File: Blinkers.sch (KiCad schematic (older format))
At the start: 242 parts, among them J1 12V, J2 A1, J3 gnd, J4 A1, J5 A1, J6 A1, J7 A1, J8 A1, Q1 Q_NMOS_DGS, Q2 Q_NMOS_DGS, Q3 Q_NMOS_DGS, Q4 Q_NMOS_DGS, Q5 Q_NMOS_DGS, Q6 Q_NMOS_DGS

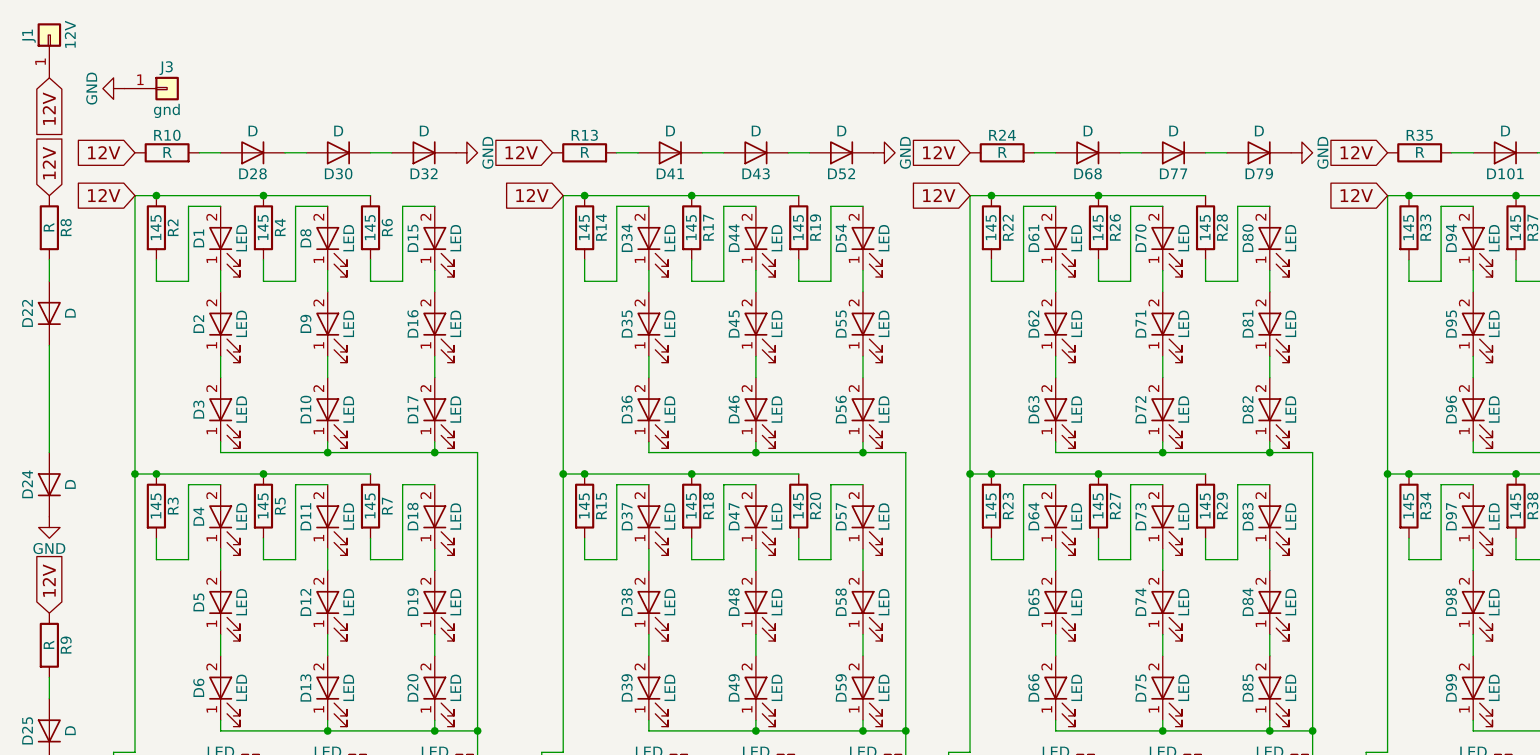
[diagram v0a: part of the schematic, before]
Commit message: Modified D_2835 to make it work with specifications for LEDs. Moved VDD and GND pins to appropriate locations near center of board.
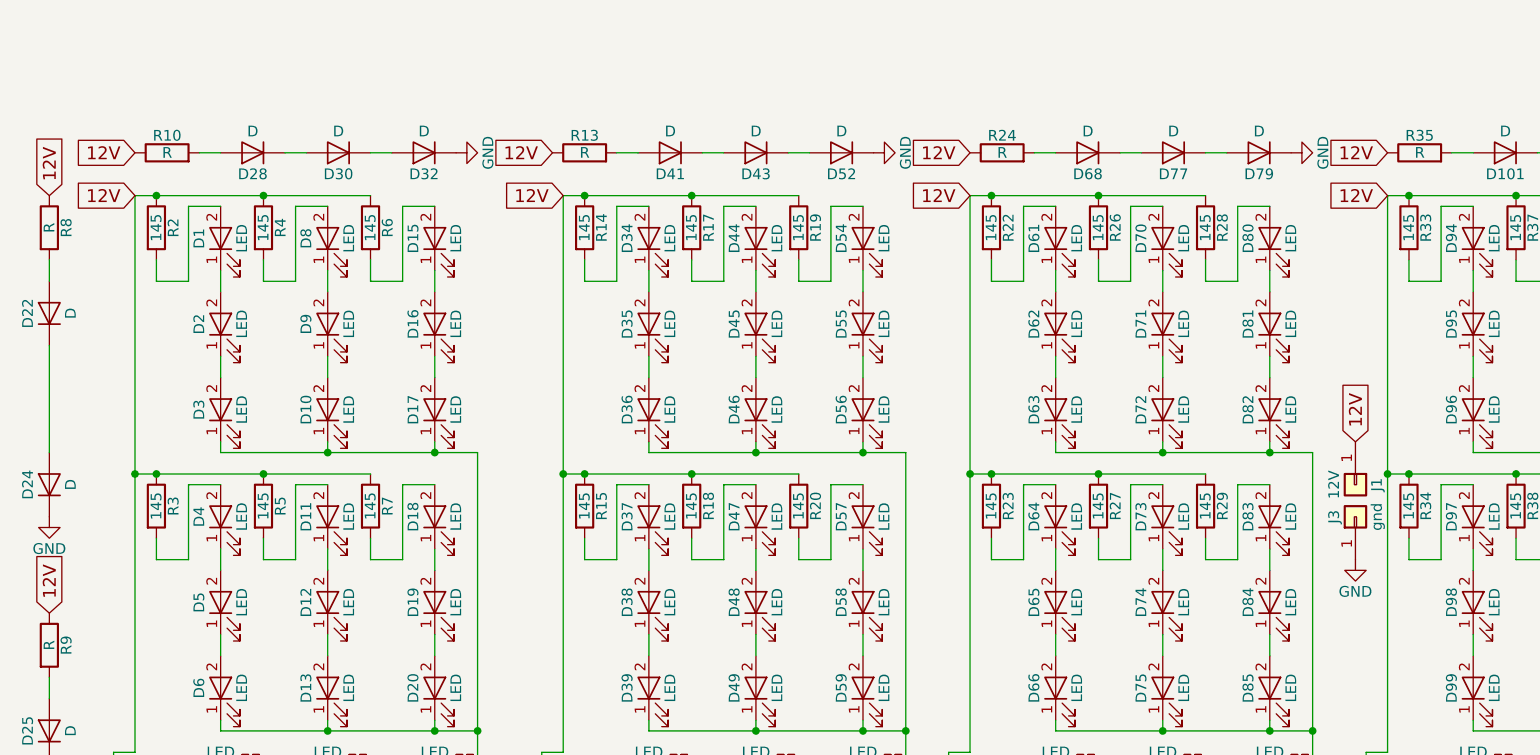
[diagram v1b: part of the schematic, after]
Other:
- moved on the sheet: J1, J3
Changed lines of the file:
@@
 L Blinkers-rescue:Conn_01x01 J1
 U 1 1 5A8E4E03
-P 800 1300
-F 0 "J1" H 800 1400 50  0000 C CNN
-F 1 "12V" H 800 1200 50  0000 C CNN
-F 2 "Socket_Strips:Socket_Strip_Straight_1x01_Pitch2.54mm" H 800 1300 50  0001 C CNN
-F 3 "" H 800 1300 50  0001 C CNN
-	1    800  1300
-	0    -1   -1   0
+P 6900 3400
+F 0 "J1" H 6900 3500 50  0000 C CNN
+F 1 "12V" H 6900 3300 50  0000 C CNN
+F 2 "Socket_Strips:Socket_Strip_Straight_1x01_Pitch2.54mm" H 6900 3400 50  0001 C CNN
+F 3 "" H 6900 3400 50  0001 C CNN
+	1    6900 3400
+	0    1    1    0
 $EndComp
 $Comp
@@
 L Blinkers-rescue:Conn_01x01 J3
 U 1 1 5A8E5EA7
-P 1350 1550
-F 0 "J3" H 1350 1650 50  0000 C CNN
-F 1 "gnd" H 1350 1450 50  0000 C CNN
-F 2 "Socket_Strips:Socket_Strip_Straight_1x01_Pitch2.54mm" H 1350 1550 50  0001 C CNN
-F 3 "" H 1350 1550 50  0001 C CNN
-	1    1350 1550
-	1    0    0    -1
+P 6900 3550
+F 0 "J3" H 6900 3650 50  0000 C CNN
+F 1 "gnd" H 6900 3450 50  0000 C CNN
+F 2 "Socket_Strips:Socket_Strip_Straight_1x01_Pitch2.54mm" H 6900 3550 50  0001 C CNN
+F 3 "" H 6900 3550 50  0001 C CNN
+	1    6900 3550
+	0    -1   -1   0
 $EndComp
-Text GLabel 800  1500 3    60   Input ~ 0
+Text GLabel 6900 3200 1    60   Input ~ 0
 12V
 Text GLabel 1200 2050 0    60   Input ~ 0
@@
 L Blinkers-rescue:GND #PWR02
 U 1 1 5A8E6C65
-P 1150 1550
-F 0 "#PWR02" H 1150 1300 50  0001 C CNN
-F 1 "GND" H 1150 1400 50  0000 C CNN
-F 2 "" H 1150 1550 50  0001 C CNN
-F 3 "" H 1150 1550 50  0001 C CNN
-	1    1150 1550
-	0    1    1    0
+P 6900 3750
+F 0 "#PWR02" H 6900 3500 50  0001 C CNN
+F 1 "GND" H 6900 3600 50  0000 C CNN
+F 2 "" H 6900 3750 50  0001 C CNN
+F 3 "" H 6900 3750 50  0001 C CNN
+	1    6900 3750
+	1    0    0    -1
 $EndComp
 $Comp

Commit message: Brake connections made in Eeschema.
"Brake" labels have been assigned to each of the outer LED strips, and a "Brake" input has been made in the center of the layout.
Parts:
- added J9: Conn_01x01, Socket_Strips:Socket_Strip_Straight_1x01_Pitch2.54mm, symbol Blinkers-rescue:Conn_01x01
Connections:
- net 12V: no longer R10.1, R11.1, R13.1, R16.1, R24.1, R25.1, R30.1, R31.1, R35.1, R36.1, R44.1, R45.1, R53.1, R54.1, R8.1, R9.1
- new net Brake: J9.1 (Pin_1), R10.1, R11.1, R13.1, R16.1, R24.1, R25.1, R30.1, R31.1, R35.1, R36.1, R44.1, R45.1, R53.1, R54.1, R8.1, R9.1
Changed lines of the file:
@@
 EESchema Schematic File Version 4
 LIBS:Blinkers-cache
-EELAYER 26 0
+EELAYER 29 0
 EELAYER END
 $Descr A3 16535 11693
@@
 Connection ~ 5100 3350
 Wire Wire Line
-	6700 3250 6700 4550
-Wire Wire Line
 	6700 4750 6650 4750
 Connection ~ 6500 3250
@@
 	800  2750 800  3250
 Text GLabel 800  2050 1    60   Input ~ 0
-12V
+Brake
 $Comp
 L Blinkers-rescue:GND #PWR05
@@
 F 3 "" H 800 3550 50  0001 C CNN
 	1    800  3550
-	1    0    0    -1
+	0    1    1    0
 $EndComp
 $Comp
@@
 	800  4700 800  5200
 Text GLabel 800  4000 1    60   Input ~ 0
-12V
+Brake
 $Comp
 L Blinkers-rescue:GND #PWR06
@@
 	2350 5600 2450 5600
 Text GLabel 1250 5600 0    60   Input ~ 0
-12V
+Brake
 $Comp
 L Blinkers-rescue:GND #PWR07
@@
 F 3 "" H 2750 5600 50  0001 C CNN
 	1    2750 5600
-	0    -1   -1   0
+	1    0    0    -1
 $EndComp
 $Comp
@@
 	4300 5600 4400 5600
 Text GLabel 3200 5600 0    60   Input ~ 0
-12V
+Brake
 $Comp
 L Blinkers-rescue:GND #PWR08
@@
 F 3 "" H 4700 5600 50  0001 C CNN
 	1    4700 5600
-	0    -1   -1   0
+	1    0    0    -1
 $EndComp
 $Comp
@@
 Wire Wire Line
 	6250 5600 6350 5600
-Text GLabel 5150 5600 0    60   Input ~ 0
-12V
 $Comp
 L Blinkers-rescue:GND #PWR09
@@
 F 3 "" H 6650 5600 50  0001 C CNN
 	1    6650 5600
-	0    -1   -1   0
+	1    0    0    -1
 $EndComp
 $Comp
@@
 	2300 1850 2400 1850
 Text GLabel 1200 1850 0    60   Input ~ 0
-12V
+Brake
 $Comp
 L Blinkers-rescue:GND #PWR010
@@
 F 3 "" H 2700 1850 50  0001 C CNN
 	1    2700 1850
-	0    -1   -1   0
+	1    0    0    -1
 $EndComp
 $Comp
@@
 	4250 1850 4350 1850
 Text GLabel 3150 1850 0    60   Input ~ 0
-12V
+Brake
 $Comp
 L Blinkers-rescue:GND #PWR011
@@
 F 3 "" H 4650 1850 50  0001 C CNN
 	1    4650 1850
-	0    -1   -1   0
+	1    0    0    -1
 $EndComp
 $Comp
@@
 	6200 1850 6300 1850
 Text GLabel 5100 1850 0    60   Input ~ 0
-12V
+Brake
 $Comp
 L Blinkers-rescue:GND #PWR012
@@
 F 3 "" H 6600 1850 50  0001 C CNN
 	1    6600 1850
-	0    -1   -1   0
+	1    0    0    -1
 $EndComp
 $Comp
@@
 	13150 2700 13150 3200
 Text GLabel 13150 2000 1    60   Input ~ 0
-12V
+Brake
 $Comp
 L Blinkers-rescue:GND #PWR013
@@
 F 3 "" H 13150 3500 50  0001 C CNN
 	1    13150 3500
-	1    0    0    -1
+	0    1    1    0
 $EndComp
 $Comp
@@
 	13150 4650 13150 5150
 Text GLabel 13150 3950 1    60   Input ~ 0
-12V
+Brake
 $Comp
 L Blinkers-rescue:GND #PWR014
@@
 	8200 5600 8300 5600
 Text GLabel 7100 5600 0    60   Input ~ 0
-12V
+Brake
 $Comp
 L Blinkers-rescue:GND #PWR016
@@
 F 3 "" H 8600 5600 50  0001 C CNN
 	1    8600 5600
-	0    -1   -1   0
+	1    0    0    -1
 $EndComp
 $Comp
@@
 	8150 1850 8250 1850
 Text GLabel 7050 1850 0    60   Input ~ 0
-12V
+Brake
 $Comp
 L Blinkers-rescue:GND #PWR017
@@
 F 3 "" H 8550 1850 50  0001 C CNN
 	1    8550 1850
-	0    -1   -1   0
+	1    0    0    -1
 $EndComp
 $Comp
@@
 	10150 5600 10250 5600
 Text GLabel 9050 5600 0    60   Input ~ 0
-12V
+Brake
 $Comp
 L Blinkers-rescue:GND #PWR019
@@
 F 3 "" H 10550 5600 50  0001 C CNN
 	1    10550 5600
-	0    -1   -1   0
+	1    0    0    -1
 $EndComp
 $Comp
@@
 	10100 1850 10200 1850
 Text GLabel 9000 1850 0    60   Input ~ 0
-12V
+Brake
 $Comp
 L Blinkers-rescue:GND #PWR020
@@
 F 3 "" H 10500 1850 50  0001 C CNN
 	1    10500 1850
-	0    -1   -1   0
+	1    0    0    -1
 $EndComp
 $Comp
@@
 Wire Wire Line
 	12100 5600 12200 5600
-Text GLabel 11000 5600 0    60   Input ~ 0
-12V
 $Comp
 L Blinkers-rescue:GND #PWR022
@@
 	12050 1850 12150 1850
 Text GLabel 10950 1850 0    60   Input ~ 0
-12V
+Brake
 $Comp
 L Blinkers-rescue:GND #PWR023
@@
 Wire Wire Line
 	11550 2050 12050 2050
+$Comp
+L Blinkers-rescue:Conn_01x01 J9
+U 1 1 5D378863
+P 6900 2900
+F 0 "J9" V 6772 2980 50  0000 L CNN
+F 1 "Conn_01x01" V 6863 2980 50  0000 L CNN
+F 2 "Socket_Strips:Socket_Strip_Straight_1x01_Pitch2.54mm" H 6900 2900 50  0001 C CNN
+F 3 "" H 6900 2900 50  0001 C CNN
+	1    6900 2900
+	0    1    1    0
+$EndComp
+Wire Wire Line
+	6700 3250 6700 4550
+Text GLabel 6900 2700 1    50   Input ~ 0
+Brake
+Text GLabel 5150 5600 0    60   Input ~ 0
+Brake
+Text GLabel 11000 5600 0    60   Input ~ 0
+Brake
 $EndSCHEMATC

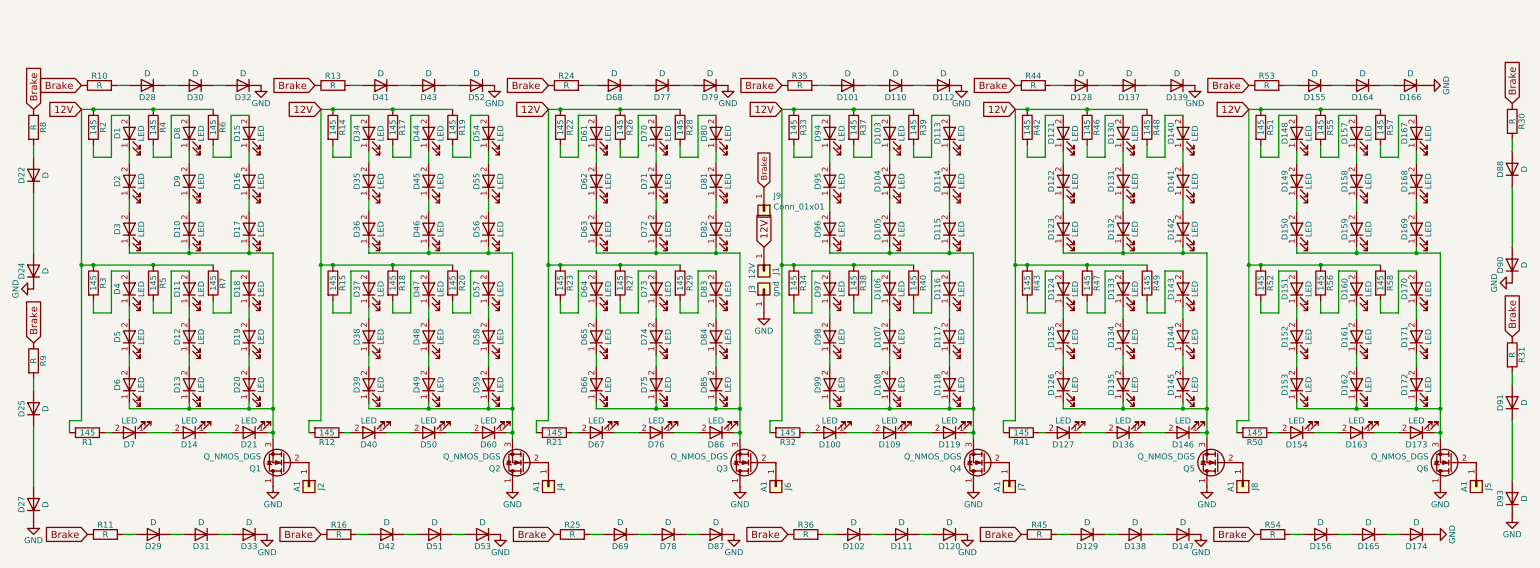
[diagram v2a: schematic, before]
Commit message: Columns and rows aligned. Outer ring aligned. Component designators assigned. VCC and GND positioned. Need to add remaining resistors and position transistors and their inputs.
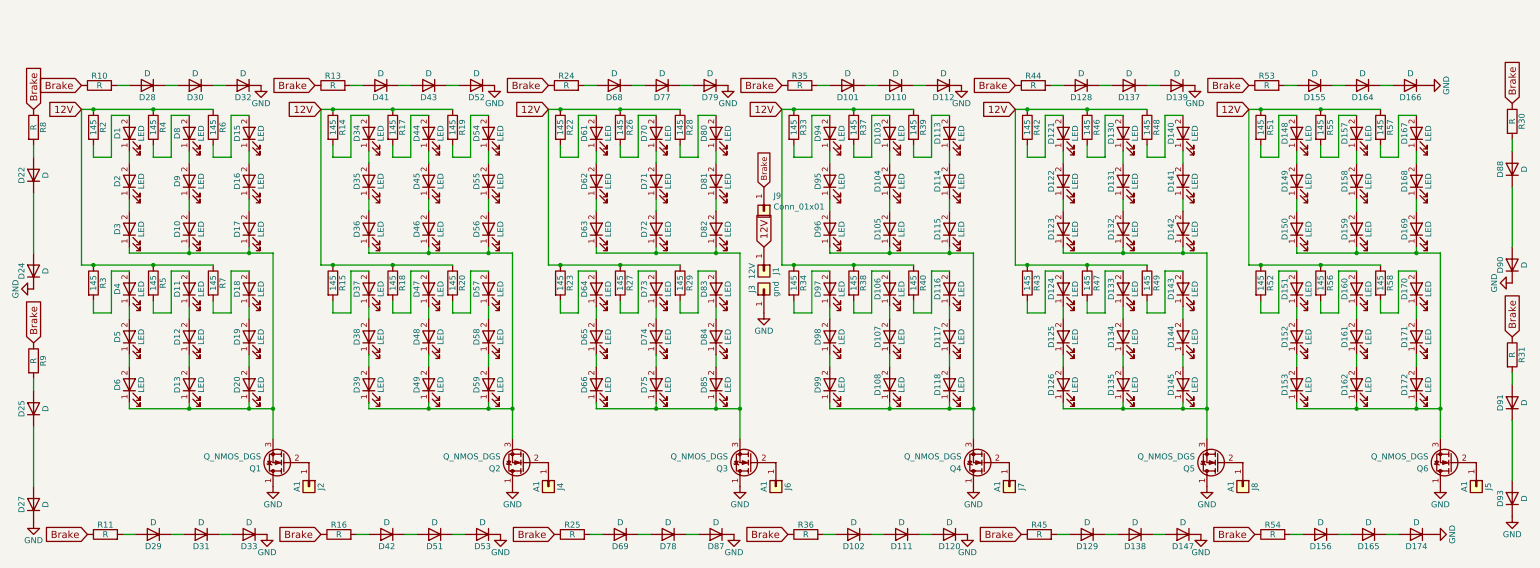
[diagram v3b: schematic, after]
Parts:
- removed D100, D109, D119, D127, D136, D14, D146, D154, D163, D173, D21, D40, D50, D60, D67, D7, D76, D86: LED, Footprints:D_2835, symbol Blinkers-rescue:LED
- removed R1, R12, R21, R32, R41, R50: 145, Resistors_SMD:R_1206, symbol Blinkers-rescue:R

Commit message: Layout complete, ready for tracerouting.
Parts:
- J9: value Conn_01x01 -> brake
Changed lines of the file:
@@
 EESchema Schematic File Version 4
 LIBS:Blinkers-cache
-EELAYER 29 0
+EELAYER 30 0
 EELAYER END
 $Descr A3 16535 11693
@@
 P 6900 2900
 F 0 "J9" V 6772 2980 50  0000 L CNN
-F 1 "Conn_01x01" V 6863 2980 50  0000 L CNN
+F 1 "brake" V 6863 2980 50  0000 L CNN
 F 2 "Socket_Strips:Socket_Strip_Straight_1x01_Pitch2.54mm" H 6900 2900 50  0001 C CNN
 F 3 "" H 6900 2900 50  0001 C CNN

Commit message: Nova_Layout_1-1
Fixed LED footprint, small pad is GND, large pad is positive. This is opposite of the data sheet.

Adjusted position of some components for better fit (and fixed R48 and R49)

Switched the input pins for the transistors to fit a 3x1 set of pins with 2.54mm pitch.

Changed inner resistor and outer resistor footprints to match original outer footprints.

Checked all reference numbers to make sure they were the correct size and will be readable when soldering.
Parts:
- D1, D10, D103, D104, D105, D106, D107, D108, D11, D113, D114, D115, D116, D117, D118, D12, D121, D122, D123, D124, D125, D126, D13, D130, D131, D132, D133, D134, D135, D140, D141, D142, D143, D144, D145, D148, D149, D15, D150, D151, D152, D153, D157, D158, D159, D16, D160, D161, D162, D167, D168, D169, D17, D170, D171, D172, D18, D19, D2, D20, D3, D34, D35, D36, D37, D38, D39, D4, D44, D45, D46, D47, D48, D49, D5, D54, D55, D56, D57, D58, D59, D6, D61, D62, D63, D64, D65, D66, D70, D71, D72, D73, D74, D75, D8, D80, D81, D82, D83, D84, D85, D9, D94, D95, D96, D97, D98, D99: footprint Footprints:D_2835 -> Footprints:D_2835_FLIPPED
- D101, D102, D110, D111, D112, D120, D128, D129, D137, D138, D139, D147, D155, D156, D164, D165, D166, D174, D22, D24, D25, D27, D28, D29, D30, D31, D32, D33, D41, D42, D43, D51, D52, D53, D68, D69, D77, D78, D79, D87, D88, D90, D91, D93: value D -> LED; footprint Footprints:D_2835 -> Footprints:D_2835_FLIPPED
- R10, R11, R13, R16, R24, R25, R30, R31, R35, R36, R44, R45, R53, R54, R8, R9: value R -> 158; footprint Resistors_SMD:R_1206 -> Blinkers_Altered_Footprints:Altered_R_1210_3225Metric
- R14, R15, R17, R18, R19, R2, R20, R22, R23, R26, R27, R28, R29, R3, R33, R34, R37, R38, R39, R4, R40, R42, R43, R46, R47, R48, R49, R5, R51, R52, R55, R56, R57, R58, R6, R7: value 145 -> 158; footprint Resistors_SMD:R_1206 -> Blinkers_Altered_Footprints:Altered_R_1210_3225Metric
